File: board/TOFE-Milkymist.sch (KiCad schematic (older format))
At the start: 6 parts, among them U7 24AA01/24LC01B, U8 TOFE-8X

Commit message: Initial version from on 2015-11-03
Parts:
- added C1, C12, C16, C2, C20, C25, C3, C9: 1uF, ~, symbol C
- added C10, C17: 100uF, ~, symbol C
- added C11, C13, C28, C30, C31, C32, C33, C34, C35, C38, C5, C7, C8: 0.1uF, ~, symbol C
- added C14: 3.3uF, ~, symbol C
- added C15: 22nF, ~, symbol C
- added C18, C24: 220uF, ~, symbol CP1
- added C19, C23: 20pF, ~, symbol C
- added C21, C22, C26, C27, C4: 220pF, ~, symbol C
- added C36, C37: 15pF, ~, symbol C
- added C39: 10uF, ~, symbol C
- added C6: 2.2uF, ~, symbol C
- added CON1, CON2, CON3, CON4: AUDIO_JACK_3535NG, ~, symbol AUDIO_JACK_3535NG
- added D1: IR-LED, ~, symbol LED
- added D2, D5, D6, D7: LED, ~, symbol LED
- added D3: DIODE, ~, symbol DIODE
- added GS1, GS2: GS2, symbol GS2
- added IC1: PC817, DIP4, symbol PC817
- added J1: DB9, symbol DB9
- added K1, K2, K5, K6, K7, K8: CONN_2, symbol CONN_2
- added K3, K4: CONN_3, symbol CONN_3
- added L1, L2, L3: 4.7uH, ~, symbol INDUCTOR_SMALL
- added P2: CONN_4X2, symbol CONN_4X2
- added P4, P5: CONN_6X2, ~, symbol CONN_6X2
- added Q1: TRANSISTOR-NPN, ~, symbol TRANSISTOR-NPN
- added R1, R24: 1K, ~, symbol R
- added R10, R9: 27.4, ~, symbol R
- added R11, R12, R13: 4.75K, ~, symbol R
- added R14: 0R, ~, symbol R
- added R16: R, ~, symbol R
- added R17: 1M, ~, symbol R
- added R18, R19, R20, R21, R33: 10K, ~, symbol R
- added R2, R3, R5, R6: 6.81K, ~, symbol R
- added R23, R7: 47R, ~, symbol R
- added R25, R26, R27, R28: 220R, ~, symbol R
- added R29: 60R, ~, symbol R
- added R30: 2K2, ~, symbol R
- added R31: 680R, ~, symbol RES_NET4
- added R32: 10K, ~, symbol RES_NET4
- added R4: 47K, ~, symbol R
- added R8: 2.2K, ~, symbol R
- added SW1, SW2, SW3, SW4: SW_PUSH, ~, symbol SW_PUSH
- added U1: LM4550, ~, symbol LM4550
- added U2: 7805_N, ~, symbol 7805_N
- added U3: ST3232CDR, ~, symbol ST3232CDR
- added U4: SN74LVC1G17, symbol SN74LVC1G17
- added U5: ISL83490, symbol ISL83490
- added U6: IR-RX, ~, symbol IR-RX
- added X1: CRYSTAL, ~, symbol CRYSTAL
- U8: value TOFE-8X -> TIMVIDEOS-PCIE-8X; symbol TOFE-8X -> TIMVIDEOS-PCIE-8X
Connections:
- net 12V: now also D4.1 (A), U8.A2 (12V), U8.A3 (12V), U8.B1 (12V), U8.B2 (12V), U8.B3 (12V); no longer D4.2 (K)
- net GND: now also C19.2, C23.2, C32.1, C33.1, C34.1, C35.2, C36.1, C37.1, C38.2, C39.1, C8.2, C9.2, D2.2 (K), D5.2 (K), D6.2 (K), D7.2 (K), IC1.3, J1.5, K1.2 (PM), K2.1 (P1), K5.2 (PM), K6.1 (P1), K8.1 (P1), P2.2, P4.10, P4.9, P5.10, P5.9, Q1.2 (E), R11.1, R12.1, R13.1, R14.1, R33.1, SW1.2, SW2.2, SW3.2, SW4.2, U1.4 (DVSS1), U1.7 (DVSS2), U3.15 (GND), U4.3 (GND), U5.4 (GND), U6.2 (GND)
- net VCC12V: now also D4.2 (K), C10.1, K3.3 (P3), U2.1 (VI); no longer D4.1 (A), U8.A2 (12V), U8.A3 (12V), U8.B1 (12V), U8.B2 (12V), U8.B3 (12V)
- net VCC3V3: now also C35.1, C38.1, C39.2, C8.1, C9.1, K4.3 (P3), K7.2 (PM), L2.1, P2.1, P4.11, P4.12, P5.11, P5.12, R23.1, R28.2, U3.16 (VCC), U5.1 (VCC)
- net RESET: now reaches U8.A11 (~RST)
- net RESET: now also R11.2, U1.11 (RESET#)
- net GPIO2: now reaches U8.A13 (DIFF_CLK_XP)
- net GPIO2: now also P2.4
- net GPIO1: now reaches U8.A14 (DIFF_CLK_XN)
- net GPIO1: now also P2.3
- net GPIO7_P: now reaches U8.A16 (DIFF_IO_A1P)
- net GPIO7_P: now also P4.1 (P1)
- net GPIO7_N: now reaches U8.A17 (DIFF_IO_A1N)
- net GPIO7_N: now also P4.2 (P2)
- net SW1: now reaches U8.A19 (DIFF_IO_YP)
- net SW1: now also R31.7
- net GPIO6_P: now reaches U8.A21 (DIFF_IO_A2P)
- net GPIO6_P: now also P4.3 (P3)
- net GPIO6_N: now reaches U8.A22 (DIFF_IO_A2N)
- net GPIO6_N: now also P4.4 (P4)
- net GPIO5_P: now reaches U8.A25 (DIFF_IO_A3P)
- net GPIO5_P: now also P4.5 (P5)
- net GPIO5_N: now reaches U8.A26 (DIFF_IO_A3N)
- net GPIO5_N: now also P4.6 (P6)
- net GPIO4_P: now reaches U8.A29 (DIFF_CLK_A0P)
- net GPIO4_P: now also P4.7 (P7)
- net GPIO4_N: now reaches U8.A30 (DIFF_CLK_A0N)
- net GPIO4_N: now also P4.8 (P8)
- net SW2: now reaches U8.A32 (DIFF_IO_ZP)
- net SW2: now also R31.5
- net GPIO3_P: now reaches U8.A35 (DIFF_IO_A4P)
- net GPIO3_P: now also P5.1 (P1)
- net GPIO3_N: now reaches U8.A36 (DIFF_IO_A4N)
- net GPIO3_N: now also P5.2 (P2)
- net GPIO2_P: now reaches U8.A39 (DIFF_IO_A5P)
- net GPIO2_P: now also P5.3 (P3)
- net GPIO2_N: now reaches U8.A40 (DIFF_IO_A5N)
- net GPIO2_N: now also P5.4 (P4)
- net GPIO1_P: now reaches U8.A43 (DIFF_IO_A6P)
- net GPIO1_P: now also P5.5 (P5)
- net GPIO1_N: now reaches U8.A44 (DIFF_IO_A6N)
- net GPIO1_N: now also P5.6 (P6)
- net GPIO0_P: now reaches U8.A47 (DIFF_CLK_A1P)
- net GPIO0_P: now also P5.7 (P7)
- net GPIO0_N: now reaches U8.A48 (DIFF_CLK_A1N)
- net GPIO0_N: now also P5.8 (P8)
- net GPIO6: now reaches U8.A5 (DIFF_IO_A0P)
- net GPIO6: now also P2.8
- net GPIO5: now reaches U8.A6 (DIFF_IO_A0N)
- net GPIO5: now also P2.7
- net GPIO4: now reaches U8.A7 (DIFF_IO_B0P)
- net GPIO4: now also P2.6
- net GPIO3: now reaches U8.A8 (DIFF_IO_B0N)
- net GPIO3: now also P2.5
- net BIT-CLK: now reaches U8.B11 (DIFF_IO_XN)
- net BIT-CLK: now also R9.1
- net AC97_SDI: now reaches U8.B12 (DIFF_IO_YN)
- net AC97_SDI: now also R10.1
- net SYNC: now reaches U8.B14 (DIFF_IO_B1P)
- net SYNC: now also R13.2, U1.10 (SYNC)
- net RS232-RX2: now reaches U8.B15 (DIFF_IO_B1N)
- net RS232-RX2: now also U3.9 (R2_OUT)
- net RS232-TX2: now reaches U8.B19 (DIFF_IO_B2P)
- net RS232-TX2: now also U3.10 (T2_IN)
- net RS232-TX1: now reaches U8.B20 (DIFF_IO_B2N)
- net RS232-TX1: now also U3.11 (T1_IN)
- net RS232-RX1: now reaches U8.B23 (DIFF_IO_B3P)
- net RS232-RX1: now also U3.12 (R1_OUT)
- net IR_EN: now reaches U8.B24 (DIFF_IO_B3N)
- net IR_EN: now also R30.1
- net IR_OUT: now reaches U8.B27 (DIFF_CLK_B0P)
- net IR_OUT: now also R24.1
- net MIDI_RX: now reaches U8.B28 (DIFF_CLK_B0N)
- net MIDI_RX: now also IC1.4, R28.1
- net MIDI_TX: now reaches U8.B30 (DIFF_IO_ZN)
- net MIDI_TX: now also U4.2 (A)
- net DMX_TX: now reaches U8.B33 (DIFF_IO_B4P)
- net DMX_TX: now also U5.2 (RO)
- net DMX_RX: now reaches U8.B34 (DIFF_IO_B4N)
- net DMX_RX: now also U5.3 (DI)
- net LED1: now reaches U8.B37 (DIFF_IO_B5P)
- net LED1: now also R32.7
- net LED2: now reaches U8.B38 (DIFF_IO_B5N)
- net LED2: now also R32.5
- net LED3: now reaches U8.B41 (DIFF_IO_B6P)
- net LED3: now also R32.3
- net LED4: now reaches U8.B42 (DIFF_IO_B6N)
- net LED4: now also R32.1
- net SW3: now reaches U8.B45 (DIFF_CLK_B1P)
- net SW3: now also R31.3
- net SW4: now reaches U8.B46 (DIFF_CLK_B1N)
- net SW4: now also R31.1
- net AC97_SDO: now reaches U8.B9 (DIFF_IO_XP)
- net AC97_SDO: now also R12.2, U1.5 (SDATA_OUT)
- new net: L2.2, U1.1 (DVDD1), U1.9 (DVDD2)
- new net: C7.2, U1.12 (PC_BEEP), U1.13 (PHONE), U1.14 (AUX_L), U1.15 (AUX_R), U1.16 (VIDEO_L), U1.17 (VIDEO_R), U1.18 (CD_L), U1.19 (CD_GND), U1.20 (CD_R), U1.22 (MIC2)
- new net: C23.1, R17.2, U1.2 (XTL_IN), X1.2
- new net: C1.2, U1.21 (MIC1)
- new net: C2.2, U1.23 (LINE_IN_L)
- new net: C3.2, U1.24 (LINE_IN_R)
- new net: C13.1, C14.1, R16.1, U1.27 (VREF)
- new net: C19.1, R17.1, U1.3 (XTL_OUT), X1.1
- new net: C15.2, U1.33 (3DN)
- new net: C15.1, U1.34 (3DP)
- new net: C20.1, U1.35 (LINE_OUT_L)
- new net: C25.1, U1.36 (LINE_OUT_R)
- new net: C18.1, U1.39 (HP_OUT_L)
- new net: C16.1, U1.40 (HP_OUT_C)
- new net: C24.1, U1.41 (HP_OUT_R)
- new net: R9.2, U1.6 (BIT_CLK)
- new net: R10.2, U1.8 (SDATA_IN)
- new net: C2.1, R2.2, R6.2
- new net: C3.1, R3.2, R5.2
- new net: CON1.2, R2.1
- new net: C18.2, C21.1, CON3.3, R18.2
- new net: CON1.3, R3.1
- new net: C24.2, C26.1, CON3.2, R20.2
- new net: C20.2, C22.1, CON4.3, R19.2
- new net: C25.2, C27.1, CON4.2, R21.2
- new net: C1.1, R1.1, R4.1
- new net: CON2.2, R1.2
- new net: CON2.3, R7.1
- new net: C4.2, R7.2, R8.1
- new net: R31.8, SW3.1
- new net: D5.1 (A), R32.8
- new net: D6.1 (A), R32.6
- new net: R31.2, SW4.1
- new net: R31.4, SW1.1
- new net: R31.6, SW2.1
- new net: D2.1 (A), R32.2
- new net: D7.1 (A), R32.4
- new net: D3.2 (K), IC1.1, R26.2
- new net: R27.2, U4.4 (Y)
- new net: C30.1, U3.3 (C1-)
- new net: C30.2, U3.1 (C1+)
- new net: C31.1, U3.5 (C2-)
- new net: C31.2, U3.4 (C2+)
- new net: C33.2, U3.2 (V+)
- new net: C32.2, U3.6 (V-)
- new net: D1.1 (A), R23.2
- new net: Q1.1 (B), R30.2, R33.2
- new net: D1.2 (K), Q1.3 (C)
- new net AGND: C10.2, C11.2, C12.2, C13.2, C14.2, C16.2, C17.2, C21.2, C22.2, C26.2, C27.2, C28.2, C4.1, C5.2, C6.1, C7.1, CON1.1 (GND), CON1.4, CON1.5, CON2.1 (GND), CON2.4, CON2.5, CON3.1 (GND), CON3.4, CON3.5, CON4.1 (GND), CON4.4, CON4.5, R14.2, R18.1, R19.1, R20.1, R21.1, R4.2, R5.1, R6.1, U1.26 (AVSS1), U2.2 (GND)
- new net AUD5V0: C11.1, C12.1, C5.1, L1.2, R16.2, U1.25 (AVDD1)
- new net AUDVREF: C6.2, R8.2, U1.28 (VREFOUT)
- new net DMX-DATA_IN+: C37.2, GS2.1 (G1), K4.1 (P1), R29.2, U5.8 (A)
- new net DMX-DATA_IN-: C36.2, GS1.1 (G1), K4.2 (PM), R29.1, U5.7 (B)
- new net DMX-DATA_OUT+: GS2.2 (G2), K6.2 (PM), U5.5 (Y)
- new net DMX-DATA_OUT-: GS1.2 (G2), K5.1 (P1), U5.6 (Z)
- new net MIDI_IN_PIN4: K3.2 (PM), R26.1
- new net MIDI_IN_PIN5: D3.1 (A), IC1.2, K3.1 (P1)
- new net MIDI_OUT_PIN4: K1.1 (P1), R25.1
- new net MIDI_OUT_PIN5: K2.2 (PM), R27.1
- new net MIDI_VCC5V0: C34.2, L3.2, R25.2, U4.5 (VCC)
- new net RS232-IN1: J1.3, U3.13 (R1_IN)
- new net RS232-IN2: K7.1 (P1), U3.8 (R2_IN)
- new net RS232-OUT1: J1.2, U3.14 (T1_OUT)
- new net RS232-OUT2: K8.2 (PM), U3.7 (T2_OUT)
- new net VCC5V0: C17.1, C28.1, L1.1, L3.1, U2.3 (VO)
- no-connect marks 1 -> 16
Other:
- note added: "0\n1\n2"
- note added: "0\n\n1\n\n"
- note added: "2\n\n3"
- note added: "3\n\n4\n"
- note added: "5\n\n6\n"
- note added: "AC'97 STEREO MODULE"
- note added: "DMX-IN"
- note added: "DMX-OUT"
- note added: "EXPANSION CONNECTORS"
- note added: "GPIO'S"
- note added: "HP OUT"
- note added: "IR RECEIVER"
- note added: "IR TRANSCEIVER"
- note added: "IR TRANSMITTER"
- note added: "LED"
- note added: "LINE IN"
- note added: "LINE OUT"
- note added: "MIC"
- note added: "MIDI IN"
- note added: "MIDI OUT"
- note added: "PCIe"
- note added: "POWER SUPPLY"
- note added: "PUSH BUTTON SWITCH"
- note added: "RS-232"
- note added: "RS-485"
- note removed: "TOFE-8x"
- moved on the sheet: C29, D4, R15, R22, U7, U8

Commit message: More changes to mechanical holes.
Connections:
- net VCC3V3: now also U6.3 (VCC)
- net at R24.2: now also U6.1 (VOUT)
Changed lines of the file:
@@
 Sheet 1 1
 Title "TOFE Milkymist Compatible Expansion Board"
-Date "2 nov 2015"
+Date "2 dec 2015"
 Rev "1.0"
 Comp "Numato Lab"
@@
 	-1   0    0    1
 $EndComp
-Wire Wire Line
-	18050 13750 18350 13750
-Wire Wire Line
-	18350 13750 18350 14000
-Text Label 18050 13750 0    60   ~ 12
+Text Label 18050 14000 0    60   ~ 12
 VCC3V3
-Wire Wire Line
-	18050 13850 18100 13850
-Wire Wire Line
-	18100 13850 18100 14450
-Wire Wire Line
-	18100 14450 18350 14450
-Wire Wire Line
-	18350 14450 18350 14400
-Text Label 18100 14450 0    60   ~ 12
+Text Label 18100 14400 0    60   ~ 12
 GND
-Wire Wire Line
-	18050 13950 18550 13950
 Wire Wire Line
 	18550 13450 18100 13450
@@
 NoConn ~ 16450 5500
 NoConn ~ 16450 4000
+Wire Wire Line
+	18050 14000 18350 14000
+Wire Wire Line
+	18050 13850 18100 13850
+Wire Wire Line
+	18100 13850 18100 14400
+Wire Wire Line
+	18100 14400 18350 14400
+Wire Wire Line
+	18050 13700 18400 13700
+Wire Wire Line
+	18400 13700 18400 13950
+Wire Wire Line
+	18400 13950 18550 13950
 $EndSCHEMATC

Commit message: Fixing part reference.
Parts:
- U8: value TIMVIDEOS-PCIE-8X -> TOFE-8X; symbol TIMVIDEOS-PCIE-8X -> TOFE-8X

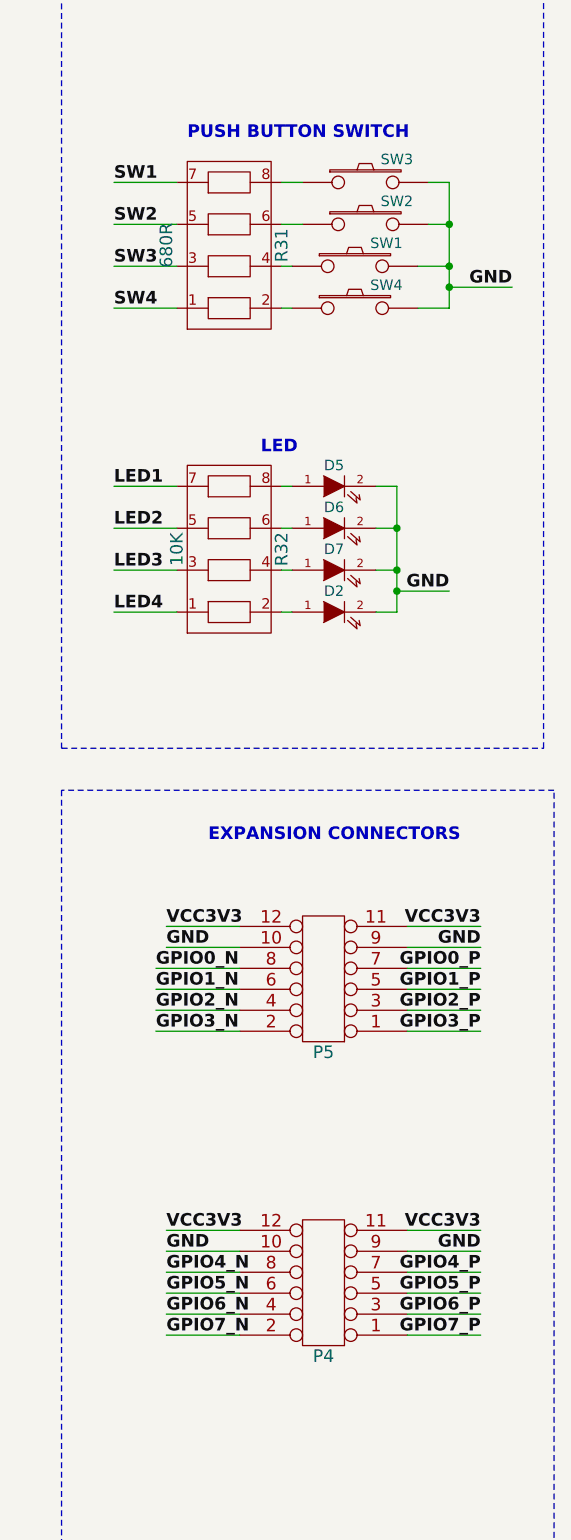
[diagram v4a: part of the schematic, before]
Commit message: Fixing switch alignment and adding extra comments.
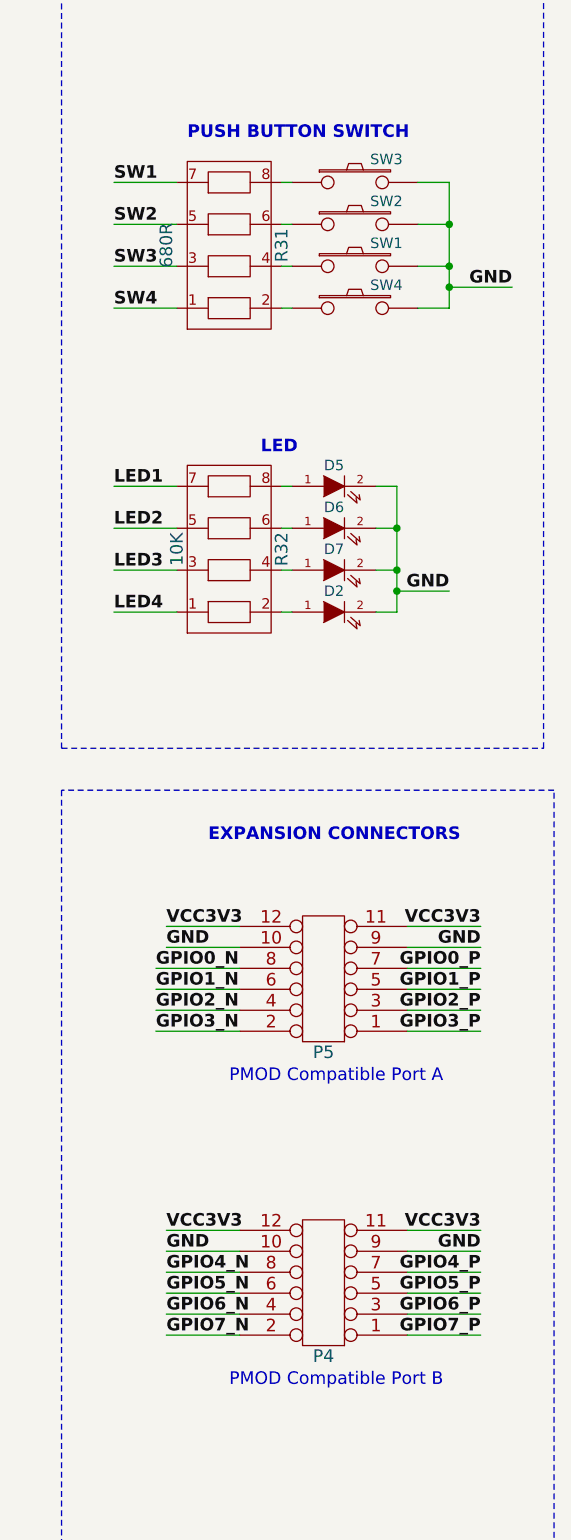
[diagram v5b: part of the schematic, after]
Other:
- note added: "PMOD Compatible Port A"
- note added: "PMOD Compatible Port B"
- moved on the sheet: SW2, SW3
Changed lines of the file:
@@
 L SW_PUSH SW3
 U 1 1 561CABBC
-P 21150 2100
-F 0 "SW3" H 21300 2210 50  0000 C CNN
-F 1 "SW_PUSH" H 21150 2020 50  0001 C CNN
-F 2 "~" H 21150 2100 60  0000 C CNN
-F 3 "~" H 21150 2100 60  0000 C CNN
-	1    21150 2100
+P 21100 2100
+F 0 "SW3" H 21250 2210 50  0000 C CNN
+F 1 "SW_PUSH" H 21100 2020 50  0001 C CNN
+F 2 "~" H 21100 2100 60  0000 C CNN
+F 3 "~" H 21100 2100 60  0000 C CNN
+	1    21100 2100
 	1    0    0    -1
 $EndComp
@@
 L SW_PUSH SW2
 U 1 1 5624BE68
-P 21150 2300
-F 0 "SW2" H 21300 2410 50  0000 C CNN
-F 1 "SW_PUSH" H 21150 2220 50  0001 C CNN
-F 2 "~" H 21150 2300 60  0000 C CNN
-F 3 "~" H 21150 2300 60  0000 C CNN
-	1    21150 2300
+P 21100 2300
+F 0 "SW2" H 21250 2410 50  0000 C CNN
+F 1 "SW_PUSH" H 21100 2220 50  0001 C CNN
+F 2 "~" H 21100 2300 60  0000 C CNN
+F 3 "~" H 21100 2300 60  0000 C CNN
+	1    21100 2300
 	1    0    0    -1
 $EndComp
@@
 Connection ~ 17700 2050
 Wire Wire Line
-	20750 2100 20850 2100
-Wire Wire Line
-	20750 2300 20850 2300
-Wire Wire Line
-	21450 2100 21550 2100
+	20750 2100 20800 2100
+Wire Wire Line
+	20750 2300 20800 2300
+Wire Wire Line
+	21400 2100 21550 2100
 Wire Wire Line
 	20250 2300 19950 2300
@@
 	21300 3950 21200 3950
 Wire Wire Line
-	21550 2300 21450 2300
+	21550 2300 21400 2300
 Wire Wire Line
 	21550 2500 21400 2500
@@
 Wire Wire Line
 	18400 13950 18550 13950
+Text Notes 20500 6400 0    60   ~ 0
+PMOD Compatible Port A
+Text Notes 20500 7850 0    60   ~ 0
+PMOD Compatible Port B
 $EndSCHEMATC

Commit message: Updated version sent to production.
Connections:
- net RS232-IN1: now also J1.2; no longer J1.3
- net RS232-OUT1: now also J1.3; no longer J1.2
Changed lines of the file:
@@
 Text Label 18300 9050 2    60   ~ 12
 GND
-Text Label 4750 14850 0    60   ~ 12
+Text Label 4750 14650 0    60   ~ 12
 RS232-OUT1
 Text Label 4250 15050 2    60   ~ 12
@@
 Text Label 4350 14450 2    60   ~ 12
 RS232-OUT1
-Text Label 4750 14650 0    60   ~ 12
+Text Label 4750 14850 0    60   ~ 12
 RS232-IN1
 Text Label 4350 14600 2    60   ~ 12
